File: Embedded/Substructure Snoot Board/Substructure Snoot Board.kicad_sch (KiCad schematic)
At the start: 23 parts, among them J3 L0 JST, J4 L1 JST, J6 A JST, J7 S Pins A, J8 S Pins B, U1 D0 FFC, U2 D1 FFC, U3 U FFC, U4 S FFC, U5 R FFC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

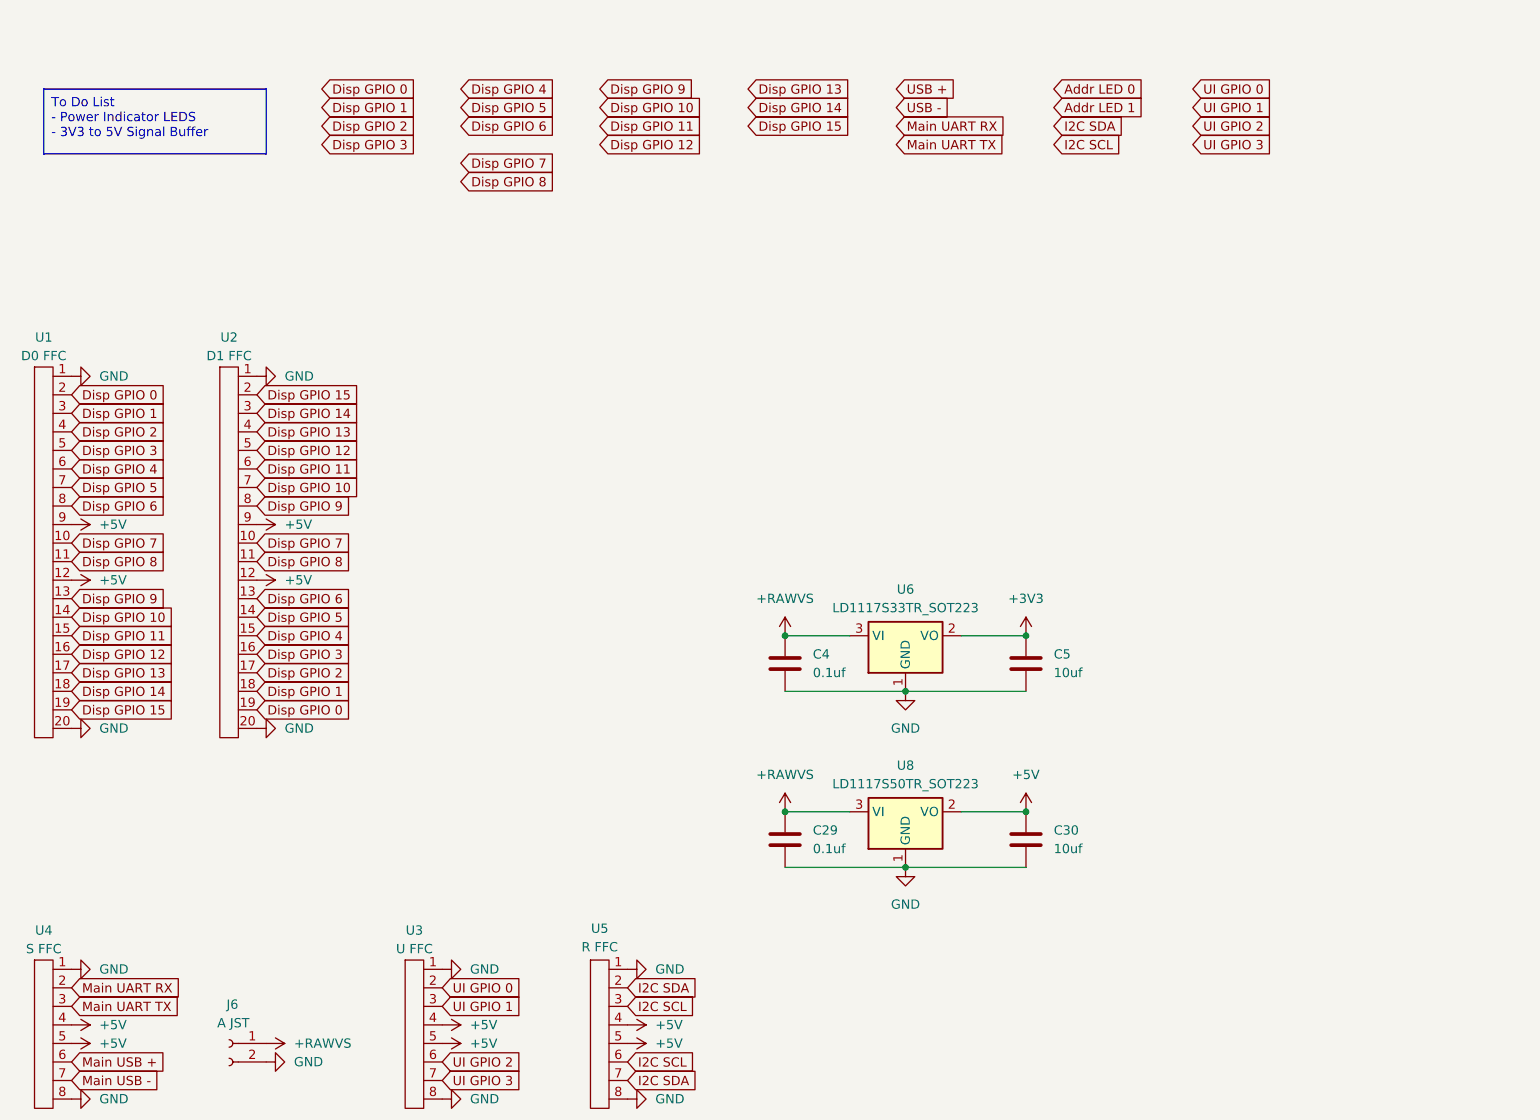
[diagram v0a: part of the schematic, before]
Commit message: Added System PWR Jumper Pins & USBC Connector & PWR Indicator LEDS
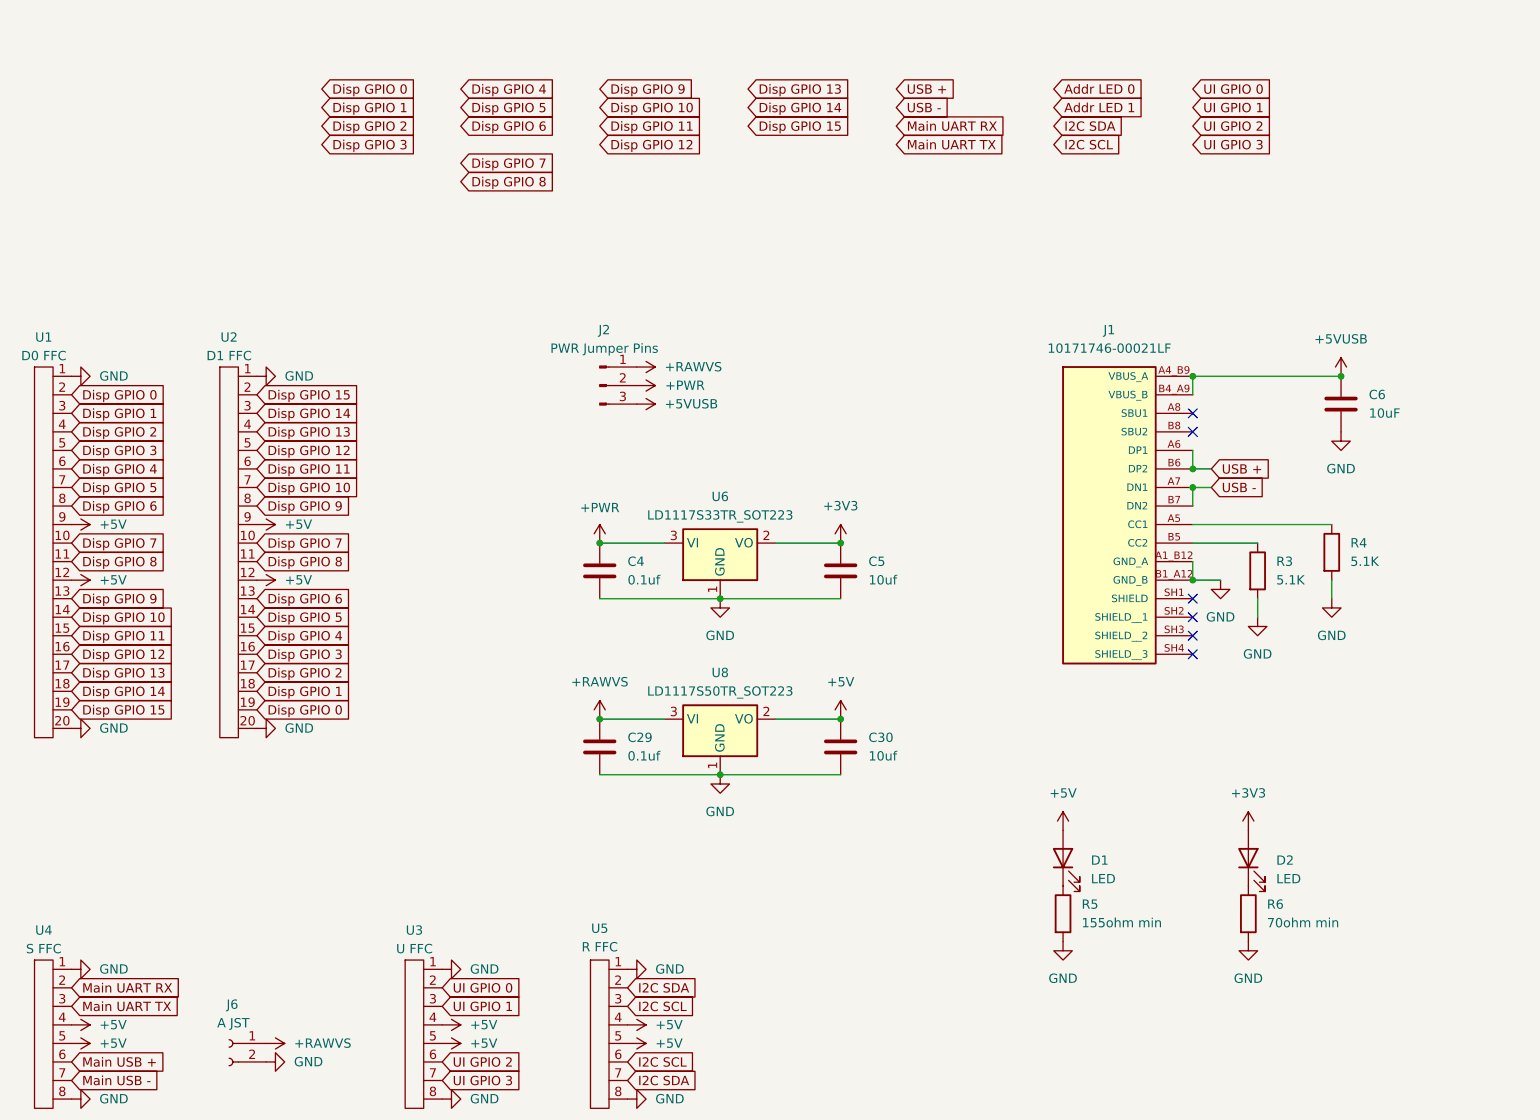
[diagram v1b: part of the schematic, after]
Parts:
- added C6: 10uF, Capacitor_SMD:C_0603_1608Metric, symbol Device:C
- added D1, D2: LED, Diode_SMD:D_0603_1608Metric_Pad1.05x0.95mm_HandSolder, symbol Device:LED
- added J1: 10171746-00021LF, USBC:AMPHENOL_10171746-00021LF, symbol USBC_10171746_00021LF:10171746-00021LF
- added J2: PWR Jumper Pins, Connector_PinHeader_2.54mm:PinHeader_1x03_P2.54mm_Horizontal, symbol Connector:Conn_01x03_Pin
- added R3, R4: 5.1K, Resistor_SMD:R_0603_1608Metric, symbol Device:R
- added R5: 155ohm min, Resistor_SMD:R_0402_1005Metric_Pad0.72x0.64mm_HandSolder, symbol Device:R
- added R6: 70ohm min, Resistor_SMD:R_0402_1005Metric_Pad0.72x0.64mm_HandSolder, symbol Device:R
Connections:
- net +3V3: now also D2.2 (A)
- net +5V: now also D1.2 (A)
- net +RAWVS: now also J2.1 (Pin_1); no longer C4.1, U6.3 (VI)
- net GND: now also C6.2, J1.A1_B12 (GND_A), J1.B1_A12 (GND_B), R3.2, R4.2, R5.2, R6.2
- net USB +: now also J1.A6 (DP1), J1.B6 (DP2)
- net USB -: now also J1.A7 (DN1), J1.B7 (DN2)
- new net: J1.A5 (CC1), R4.1
- new net: J1.B5 (CC2), R3.1
- new net: D1.1 (K), R5.1
- new net: D2.1 (K), R6.1
- new net +5VUSB: C6.1, J1.A4_B9 (VBUS_A), J1.B4_A9 (VBUS_B), J2.3 (Pin_3)
- new net +PWR: C4.1, J2.2 (Pin_2), U6.3 (VI)
- no-connect marks 6 -> 12
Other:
- moved on the sheet: C29, C30, C4, C5, U6, U8

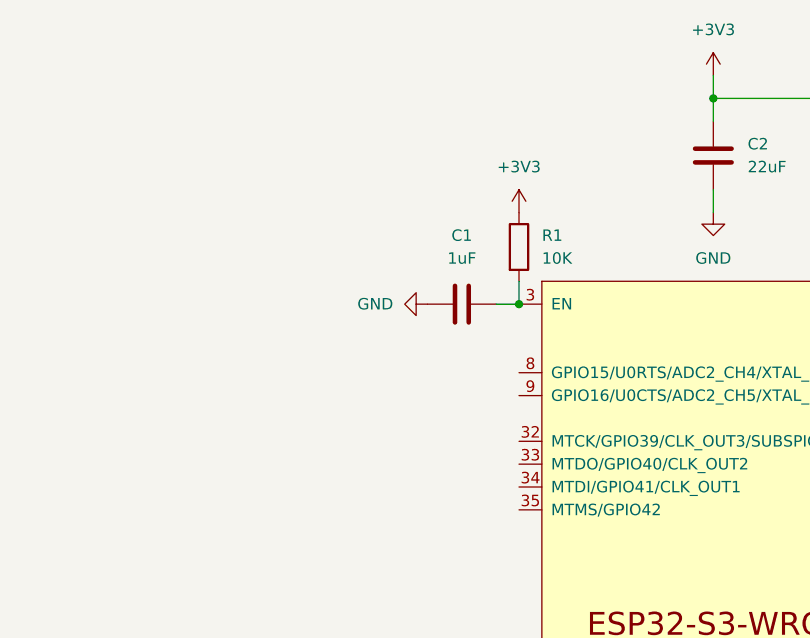
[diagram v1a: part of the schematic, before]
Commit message: Added RST Button
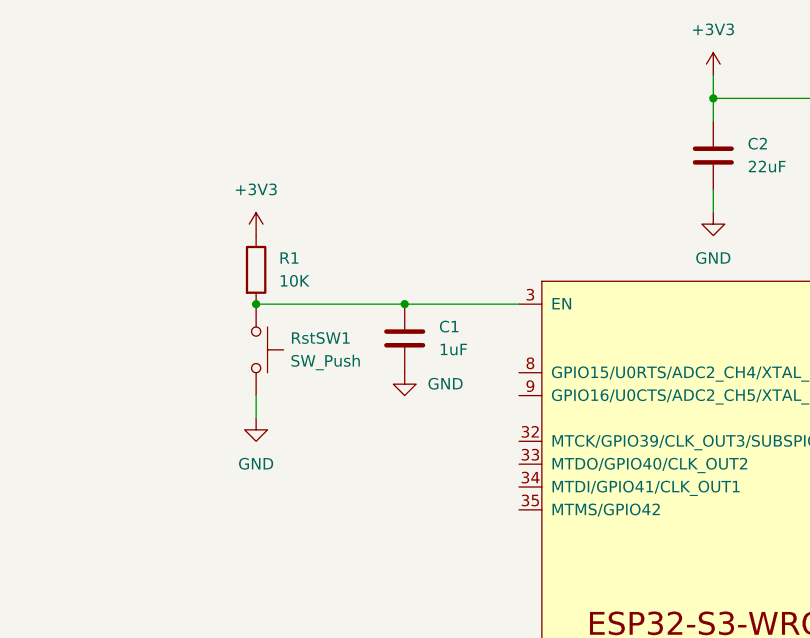
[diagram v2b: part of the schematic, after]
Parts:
- added RstSW1: SW_Push, Buttons:R-667843, symbol Switch:SW_Push
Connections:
- net GND: now also RstSW1.2
- net at C1.2, ESP1.3 (EN), R1.2: now also RstSW1.1
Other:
- moved on the sheet: C1, R1
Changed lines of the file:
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@@
 	)
 	(junction
+		(at 271.78 46.99)
+		(diameter 0)
+		(color 0 0 0 0)
+	)
+	(junction
 		(at 134.62 111.76)
 		(diameter 0)
@@
 	)
 	(junction
-		(at 284.48 46.99)
+		(at 320.04 24.13)
 		(diameter 0)
 		(color 0 0 0 0)
 	)
 	(junction
-		(at 320.04 24.13)
+		(at 118.11 119.38)
 		(diameter 0)
 		(color 0 0 0 0)
 	)
 	(junction
-		(at 118.11 119.38)
+		(at 101.6 111.76)
 		(diameter 0)
 		(color 0 0 0 0)
 	)
 	(junction
-		(at 101.6 111.76)
+		(at 255.27 46.99)
 		(diameter 0)
 		(color 0 0 0 0)
@@
 	(wire
 		(pts
-			(xy 284.48 44.45) (xy 284.48 46.99)
-		)
-		(stroke
-			(width 0)
-			(type default)
-		)
-	)
-	(wire
-		(pts
 			(xy 182.88 74.93) (xy 182.88 77.47)
 		)
@@
 	(wire
 		(pts
-			(xy 281.94 46.99) (xy 284.48 46.99)
+			(xy 375.92 62.23) (xy 394.97 62.23)
 		)
 		(stroke
@@
 	(wire
 		(pts
-			(xy 375.92 62.23) (xy 394.97 62.23)
+			(xy 255.27 59.69) (xy 255.27 57.15)
 		)
 		(stroke
@@
 	(wire
 		(pts
+			(xy 271.78 46.99) (xy 284.48 46.99)
+		)
+		(stroke
+			(width 0)
+			(type default)
+		)
+	)
+	(wire
+		(pts
 			(xy 101.6 95.25) (xy 118.11 95.25)
 		)
@@
 	(wire
 		(pts
+			(xy 255.27 46.99) (xy 271.78 46.99)
+		)
+		(stroke
+			(width 0)
+			(type default)
+		)
+	)
+	(wire
+		(pts
 			(xy 394.97 74.93) (xy 394.97 72.39)
 		)
@@
 	(symbol
 		(lib_id "power:GND")
-		(at 274.32 46.99 270)
+		(at 271.78 54.61 0)
 		(unit 1)
 		(exclude_from_sim no)
@@
 		(fields_autoplaced yes)
 		(property "Reference" "#PWR09"
-			(at 267.97 46.99 0)
+			(at 271.78 60.96 0)
 			(effects
 				(font
@@
 		)
 		(property "Value" "GND"
-			(at 270.51 46.9899 90)
+			(at 274.32 55.8799 0)
 			(effects
 				(font
 					(size 1.27 1.27)
 				)
-				(justify right)
+				(justify left)
 			)
 		)
 		(property "Footprint" ""
-			(at 274.32 46.99 0)
+			(at 271.78 54.61 0)
 			(effects
 				(font
@@
 		)
 		(property "Datasheet" ""
-			(at 274.32 46.99 0)
+			(at 271.78 54.61 0)
 			(effects
 				(font
@@
 		)
 		(property "Description" "Power symbol creates a global label with name \"GND\" , ground"
-			(at 274.32 46.99 0)
+			(at 271.78 54.61 0)
 			(effects
 				(font
@@
 	(symbol
 		(lib_id "Device:R")
-		(at 284.48 40.64 0)
+		(at 255.27 43.18 0)
 		(unit 1)
 		(exclude_from_sim no)
@@
 		(fields_autoplaced yes)
 		(property "Reference" "R1"
-			(at 287.02 39.3699 0)
+			(at 257.81 41.9099 0)
 			(effects
 				(font
@@
 		)
 		(property "Value" "10K"
-			(at 287.02 41.9099 0)
+			(at 257.81 44.4499 0)
 			(effects
 				(font
@@
 		)
 		(property "Footprint" "Resistor_SMD:R_0603_1608Metric"
-			(at 282.702 40.64 90)
+			(at 253.492 43.18 90)
 			(effects
 				(font
@@
 		)
 		(property "Datasheet" "~"
-			(at 284.48 40.64 0)
+			(at 255.27 43.18 0)
 			(effects
 				(font
@@
 		)
 		(property "Description" "Resistor"
-			(at 284.48 40.64 0)
+			(at 255.27 43.18 0)
 			(effects
 				(font
@@
 		)
 		(property "Sim.Device" ""
-			(at 284.48 40.64 0)
+			(at 255.27 43.18 0)
 			(effects
 				(font
@@
 		)
 		(property "Sim.Pins" ""
-			(at 284.48 40.64 0)
+			(at 255.27 43.18 0)
 			(effects
 				(font
@@
 	(symbol
 		(lib_id "power:+3V3")
-		(at 284.48 36.83 0)
+		(at 255.27 39.37 0)
 		(unit 1)
 		(exclude_from_sim no)
@@
 		(fields_autoplaced yes)
 		(property "Reference" "#PWR010"
-			(at 284.48 40.64 0)
+			(at 255.27 43.18 0)
 			(effects
 				(font
@@
 		)
 		(property "Value" "+3V3"
-			(at 284.48 31.75 0)
+			(at 255.27 34.29 0)
 			(effects
 				(font
@@
 		)
 		(property "Footprint" ""
-			(at 284.48 36.83 0)
+			(at 255.27 39.37 0)
 			(effects
 				(font
@@
 		)
 		(property "Datasheet" ""
-			(at 284.48 36.83 0)
+			(at 255.27 39.37 0)
 			(effects
 				(font
@@
 		)
 		(property "Description" "Power symbol creates a global label with name \"+3V3\""
-			(at 284.48 36.83 0)
+			(at 255.27 39.37 0)
 			(effects
 				(font
@@
 	)
 	(symbol
+		(lib_id "power:GND")
+		(at 255.27 59.69 0)
+		(unit 1)
+		(exclude_from_sim no)
+		(in_bom yes)
+		(on_board yes)
+		(dnp no)
+		(fields_autoplaced yes)
+		(property "Reference" "#PWR048"
+			(at 255.27 66.04 0)
+			(effects
+				(font
+					(size 1.27 1.27)
+				)
+				(hide yes)
+			)
+		)
+		(property "Value" "GND"
+			(at 255.27 64.77 0)
+			(effects
+				(font
+					(size 1.27 1.27)
+				)
+			)
+		)
+		(property "Footprint" ""
+			(at 255.27 59.69 0)
+			(effects
+				(font
+					(size 1.27 1.27)
+				)
+				(hide yes)
+			)
+		)
+		(property "Datasheet" ""
+			(at 255.27 59.69 0)
+			(effects
+				(font
+					(size 1.27 1.27)
+				)
+				(hide yes)
+			)
+		)
+		(property "Description" "Power symbol creates a global label with name \"GND\" , ground"
+			(at 255.27 59.69 0)
+			(effects
+				(font
+					(size 1.27 1.27)
+				)
+				(hide yes)
+			)
+		)
+		(pin "1"
+		)
+		(instances
+			(project "Substructure Snoot Board"
+				(path "/f2fe47b0-47e9-4c85-8000-2f6998edcf1c"
+					(reference "#PWR048")
+					(unit 1)
+				)
+			)
+		)
+	)
+	(symbol
 		(lib_id "power:+5VP")
 		(at 101.6 87.63 0)
@@
 	(symbol
 		(lib_id "Device:C")
-		(at 278.13 46.99 90)
+		(at 271.78 50.8 180)
 		(unit 1)
 		(exclude_from_sim no)
@@
 		(fields_autoplaced yes)
 		(property "Reference" "C1"
-			(at 278.13 39.37 90)
+			(at 275.59 49.5299 0)
 			(effects
 				(font
 					(size 1.27 1.27)
 				)
+				(justify right)
 			)
 		)
 		(property "Value" "1uF"
-			(at 278.13 41.91 90)
+			(at 275.59 52.0699 0)
 			(effects
 				(font
 					(size 1.27 1.27)
 				)
+				(justify right)
 			)
 		)
 		(property "Footprint" "Capacitor_SMD:C_0603_1608Metric"
-			(at 281.94 46.0248 0)
+			(at 270.8148 46.99 0)
 			(effects
 				(font
@@
 		)
 		(property "Datasheet" "~"
-			(at 278.13 46.99 0)
+			(at 271.78 50.8 0)
 			(effects
 				(font
@@
 		)
 		(property "Description" "Unpolarized capacitor"
-			(at 278.13 46.99 0)
+			(at 271.78 50.8 0)
 			(effects
 				(font
@@
 		)
 		(property "Sim.Device" ""
-			(at 278.13 46.99 0)
+			(at 271.78 50.8 0)
 			(effects
 				(font
@@
 		)
 		(property "Sim.Pins" ""
-			(at 278.13 46.99 0)
+			(at 271.78 50.8 0)
 			(effects
 				(font
@@
 					(unit 1)
 				)
+			)
+		)
+	)
+	(symbol
+		(lib_id "Switch:SW_Push")
+		(at 255.27 52.07 270)
+		(unit 1)
+		(exclude_from_sim no)
+		(in_bom yes)
+		(on_board yes)
+		(dnp no)
+		(fields_autoplaced yes)
+		(property "Reference" "RstSW1"
+			(at 259.08 50.7999 90)
+			(effects
+				(font
+					(size 1.27 1.27)
+				)
+				(justify left)
+			)
+		)
+		(property "Value" "SW_Push"
+			(at 259.08 53.3399 90)
+			(effects
+				(font
+					(size 1.27 1.27)
+				)
+				(justify left)
+			)
+		)
+		(property "Footprint" "Buttons:R-667843"
+			(at 260.35 52.07 0)
+			(effects
+				(font
+					(size 1.27 1.27)
+				)
+				(hide yes)
+			)
+		)
+		(property "Datasheet" "~"
+			(at 260.35 52.07 0)
+			(effects
+				(font
+					(size 1.27 1.27)
+				)
+				(hide yes)
+			)
+		)
+		(property "Description" "Push button switch, generic, two pins"
+			(at 255.27 52.07 0)
+			(effects
+				(font
+					(size 1.27 1.27)
+				)
+				(hide yes)
+			)
+		)
+		(property "Sim.Device" ""
+			(at 255.27 52.07 0)
+			(effects
+				(font
+					(size 1.27 1.27)
+				)
+				(hide yes)
+			)
+		)
+		(property "Sim.Pins" ""
+			(at 255.27 52.07 0)
+			(effects
+				(font
+					(size 1.27 1.27)
+				)
+				(hide yes)
+			)
+		)
+		(pin "1"
+		)
+		(pin "2"
+		)
+		(instances
+			(project "Substructure Snoot Board"
+				(path "/f2fe47b0-47e9-4c85-8000-2f6998edcf1c"
+					(reference "RstSW1")
+					(unit 1)
+				)
